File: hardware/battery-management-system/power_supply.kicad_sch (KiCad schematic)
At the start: 34 parts, among them U2 L6982CDR, U3 L6982CDR, U4 ICL7660, U5 ICL7660

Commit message: update symbols from library
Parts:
- R10, R14: Mouser Part Number (none) -> 603-RC0603FR-1039KL
- R11, R7: Mouser Part Number (none) -> 603-RT0603FRE07390KL
- R12, R8: Mouser Part Number (none) -> 652-CR0603FX-1002ELF
- R13: Mouser Part Number (none) -> 603-RT0603FRE0743KL
- R9: Mouser Part Number (none) -> 603-RT0603FRE13100KL
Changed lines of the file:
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@@
 			)
 		)
+		(property "Mouser Part Number" "652-CR0603FX-1002ELF"
+			(at 144.78 85.09 0)
+			(effects
+				(font
+					(size 1.27 1.27)
+				)
+				(hide yes)
+			)
+		)
 		(pin "1"
 		)
@@
 			)
 		)
+		(property "Mouser Part Number" "603-RT0603FRE07390KL"
+			(at 144.78 24.13 0)
+			(effects
+				(font
+					(size 1.27 1.27)
+				)
+				(hide yes)
+			)
+		)
 		(pin "1"
 		)
@@
 			)
 		)
+		(property "Mouser Part Number" "603-RT0603FRE07390KL"
+			(at 144.78 76.2 0)
+			(effects
+				(font
+					(size 1.27 1.27)
+				)
+				(hide yes)
+			)
+		)
 		(pin "1"
 		)
@@
 			)
 		)
+		(property "Mouser Part Number" "603-RC0603FR-1039KL"
+			(at 144.78 104.14 0)
+			(effects
+				(font
+					(size 1.27 1.27)
+				)
+				(hide yes)
+			)
+		)
 		(pin "1"
 		)
@@
 			)
 		)
+		(property "Mouser Part Number" "603-RT0603FRE13100KL"
+			(at 144.78 43.18 0)
+			(effects
+				(font
+					(size 1.27 1.27)
+				)
+				(hide yes)
+			)
+		)
 		(pin "1"
 		)
@@
 			)
 		)
+		(property "Mouser Part Number" "603-RC0603FR-1039KL"
+			(at 144.78 52.07 0)
+			(effects
+				(font
+					(size 1.27 1.27)
+				)
+				(hide yes)
+			)
+		)
 		(pin "1"
 		)
@@
 			)
 		)
+		(property "Mouser Part Number" "603-RT0603FRE0743KL"
+			(at 144.78 95.25 0)
+			(effects
+				(font
+					(size 1.27 1.27)
+				)
+				(hide yes)
+			)
+		)
 		(pin "1"
 		)
@@
 			(at 144.78 33.02 0)
 			(effects
+				(font
+					(size 1.27 1.27)
+				)
+				(hide yes)
+			)
+		)
+		(property "Mouser Part Number" "652-CR0603FX-1002ELF"
+			(at 144.78 33.02 0)
+			(effects

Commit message: update symbols from library
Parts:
- D10, D11, D4, D5, D6, D7, D8, D9: Mouser Part Number (none) -> 637-BAT54WS
- U2, U3: Mouser Part Number (none) -> 511-L6982CDR
- U4, U5: Mouser Part Number (none) -> 968-ICL7660CBAZ-T
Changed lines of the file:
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@@
 			)
 		)
+		(property "Mouser Part Number" "637-BAT54WS"
+			(at 76.454 134.62 0)
+			(effects
+				(font
+					(size 1.27 1.27)
+				)
+				(hide yes)
+			)
+		)
 		(pin "1"
 		)
@@
 			)
 		)
+		(property "Mouser Part Number" "637-BAT54WS"
+			(at 212.344 77.47 0)
+			(effects
+				(font
+					(size 1.27 1.27)
+				)
+				(hide yes)
+			)
+		)
 		(pin "1"
 		)
@@
 			)
 		)
+		(property "Mouser Part Number" "637-BAT54WS"
+			(at 129.794 134.62 0)
+			(effects
+				(font
+					(size 1.27 1.27)
+				)
+				(hide yes)
+			)
+		)
 		(pin "1"
 		)
@@
 			)
 		)
+		(property "Mouser Part Number" "968-ICL7660CBAZ-T"
+			(at 40.64 142.24 0)
+			(effects
+				(font
+					(size 1.27 1.27)
+				)
+				(hide yes)
+			)
+		)
 		(pin "3"
 		)
@@
 			)
 		)
+		(property "Mouser Part Number" "511-L6982CDR"
+			(at 106.68 26.67 0)
+			(effects
+				(font
+					(size 1.27 1.27)
+				)
+				(hide yes)
+			)
+		)
 		(pin "1"
 		)
@@
 			)
 		)
+		(property "Mouser Part Number" "637-BAT54WS"
+			(at 52.324 30.48 0)
+			(effects
+				(font
+					(size 1.27 1.27)
+				)
+				(hide yes)
+			)
+		)
 		(pin "1"
 		)
@@
 			)
 		)
+		(property "Mouser Part Number" "637-BAT54WS"
+			(at 160.274 134.62 0)
+			(effects
+				(font
+					(size 1.27 1.27)
+				)
+				(hide yes)
+			)
+		)
 		(pin "1"
 		)
@@
 			)
 		)
+		(property "Mouser Part Number" "968-ICL7660CBAZ-T"
+			(at 124.46 142.24 0)
+			(effects
+				(font
+					(size 1.27 1.27)
+				)
+				(hide yes)
+			)
+		)
 		(pin "3"
 		)
@@
 			)
 		)
+		(property "Mouser Part Number" "637-BAT54WS"
+			(at 212.344 87.63 0)
+			(effects
+				(font
+					(size 1.27 1.27)
+				)
+				(hide yes)
+			)
+		)
 		(pin "1"
 		)
@@
 			)
 		)
+		(property "Mouser Part Number" "637-BAT54WS"
+			(at 52.324 40.64 0)
+			(effects
+				(font
+					(size 1.27 1.27)
+				)
+				(hide yes)
+			)
+		)
 		(pin "1"
 		)
@@
 			)
 		)
+		(property "Mouser Part Number" "637-BAT54WS"
+			(at 45.974 134.62 0)
+			(effects
+				(font
+					(size 1.27 1.27)
+				)
+				(hide yes)
+			)
+		)
 		(pin "1"
 		)
@@
 			(at 106.68 78.74 0)
 			(effects
+				(font
+					(size 1.27 1.27)
+				)
+				(hide yes)
+			)
+		)
+		(property "Mouser Part Number" "511-L6982CDR"
+			(at 106.68 78.74 0)
+			(effects

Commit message: replace reset button, update symbols
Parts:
- L1, L2: Mouser Part Number (none) -> 580-13R223C
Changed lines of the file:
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@@
+			)
+		)
+		(property "Mouser Part Number" "580-13R223C"
+			(at 156.21 20.32 0)
+			(effects
+				(font
+					(size 1.27 1.27)
+				)
+				(hide yes)
 			)
 		)
@@
 			(at 156.21 72.39 0)
 			(effects
+				(font
+					(size 1.27 1.27)
+				)
+				(hide yes)
+			)
+		)
+		(property "Mouser Part Number" "580-13R223C"
+			(at 156.21 72.39 0)
+			(effects

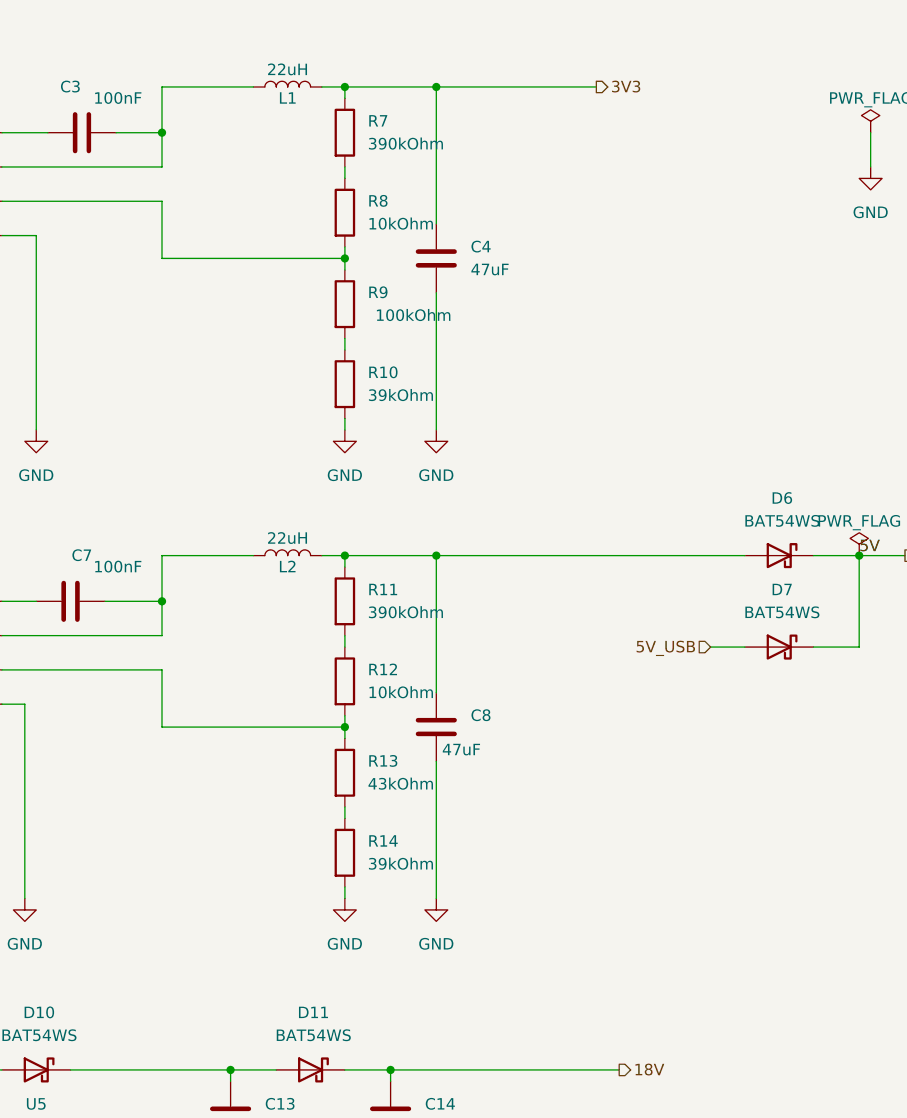
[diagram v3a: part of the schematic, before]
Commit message: replace inductance of power supplies
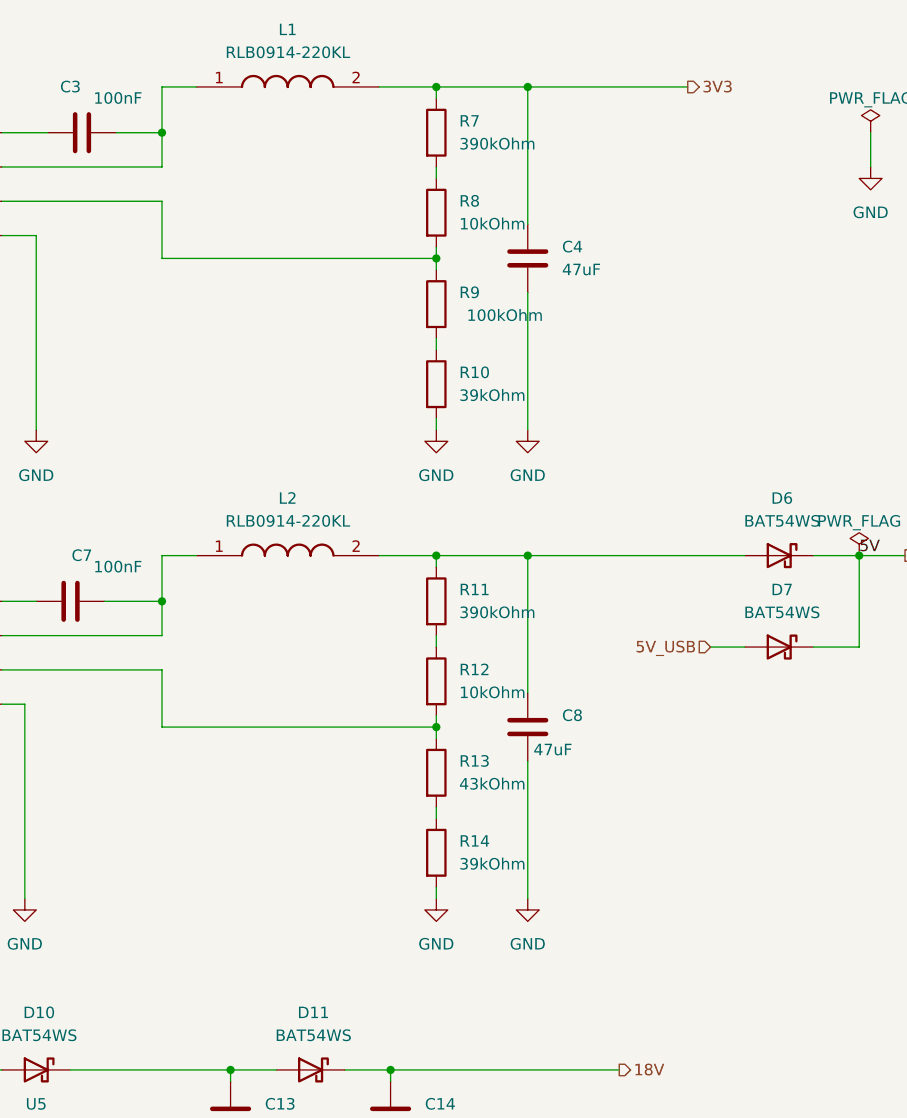
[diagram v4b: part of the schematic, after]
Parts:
- removed L1, L2: 22uH, benediktibk:L_Radial_D9.5mm_P5.00mm_Fastron_07HVP, symbol benediktibk:L_22uH_1_9A_9MHz_10%
- added L1, L2: RLB0914-220KL, benediktibk:RLB0914220KL, symbol benediktibk:RLB0914-220KL
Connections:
- net 3V3: now also L1.2
- net at C8.1, D6.2 (A), R11.1: now also L2.2
- net at C7.1, U3.1 (SW): now also L2.1
- net at C3.1, U2.1 (SW): now also L1.1
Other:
- moved on the sheet: C4, C8, R10, R11, R12, R13, R14, R7, R8, R9
